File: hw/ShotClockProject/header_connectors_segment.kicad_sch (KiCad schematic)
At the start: 4 parts, among them J4 Conn_01x33_Pin, J5 Conn_01x33_Pin, J6 Conn_01x33_Pin, J7 Conn_01x33_Pin

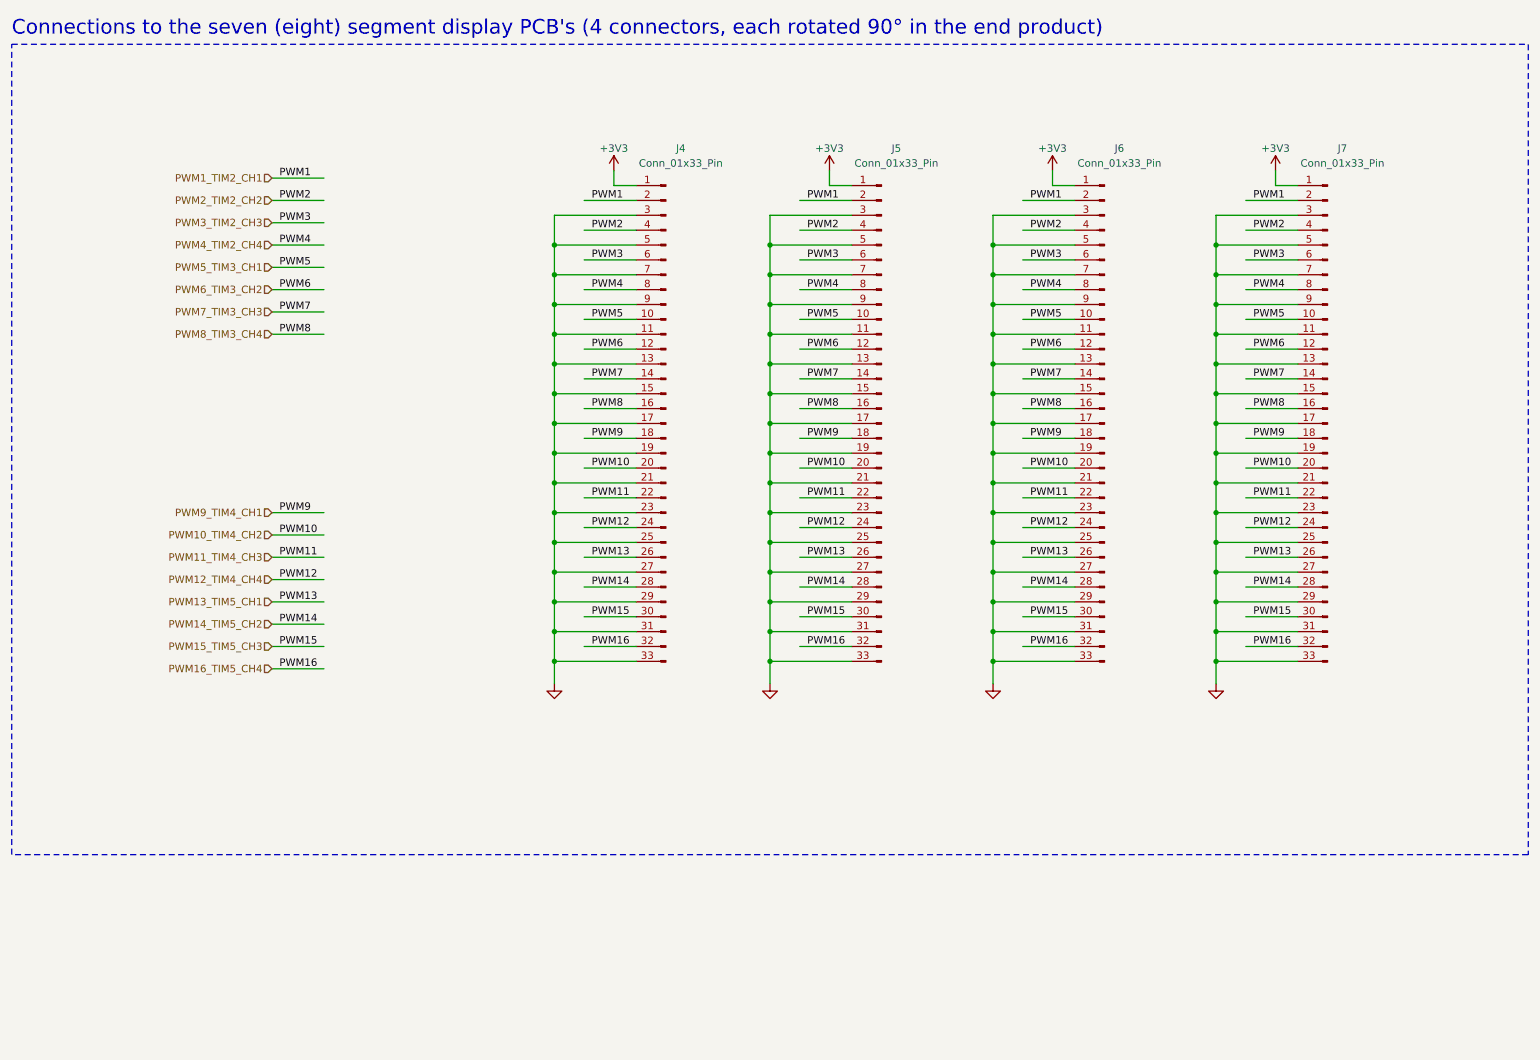
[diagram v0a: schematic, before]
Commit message: Fixed all ERC issues
Mainly by placing PWR_FLAGs and NetTies to show KiCAD where the GNDs are connected to each other physically, without them being the same net.
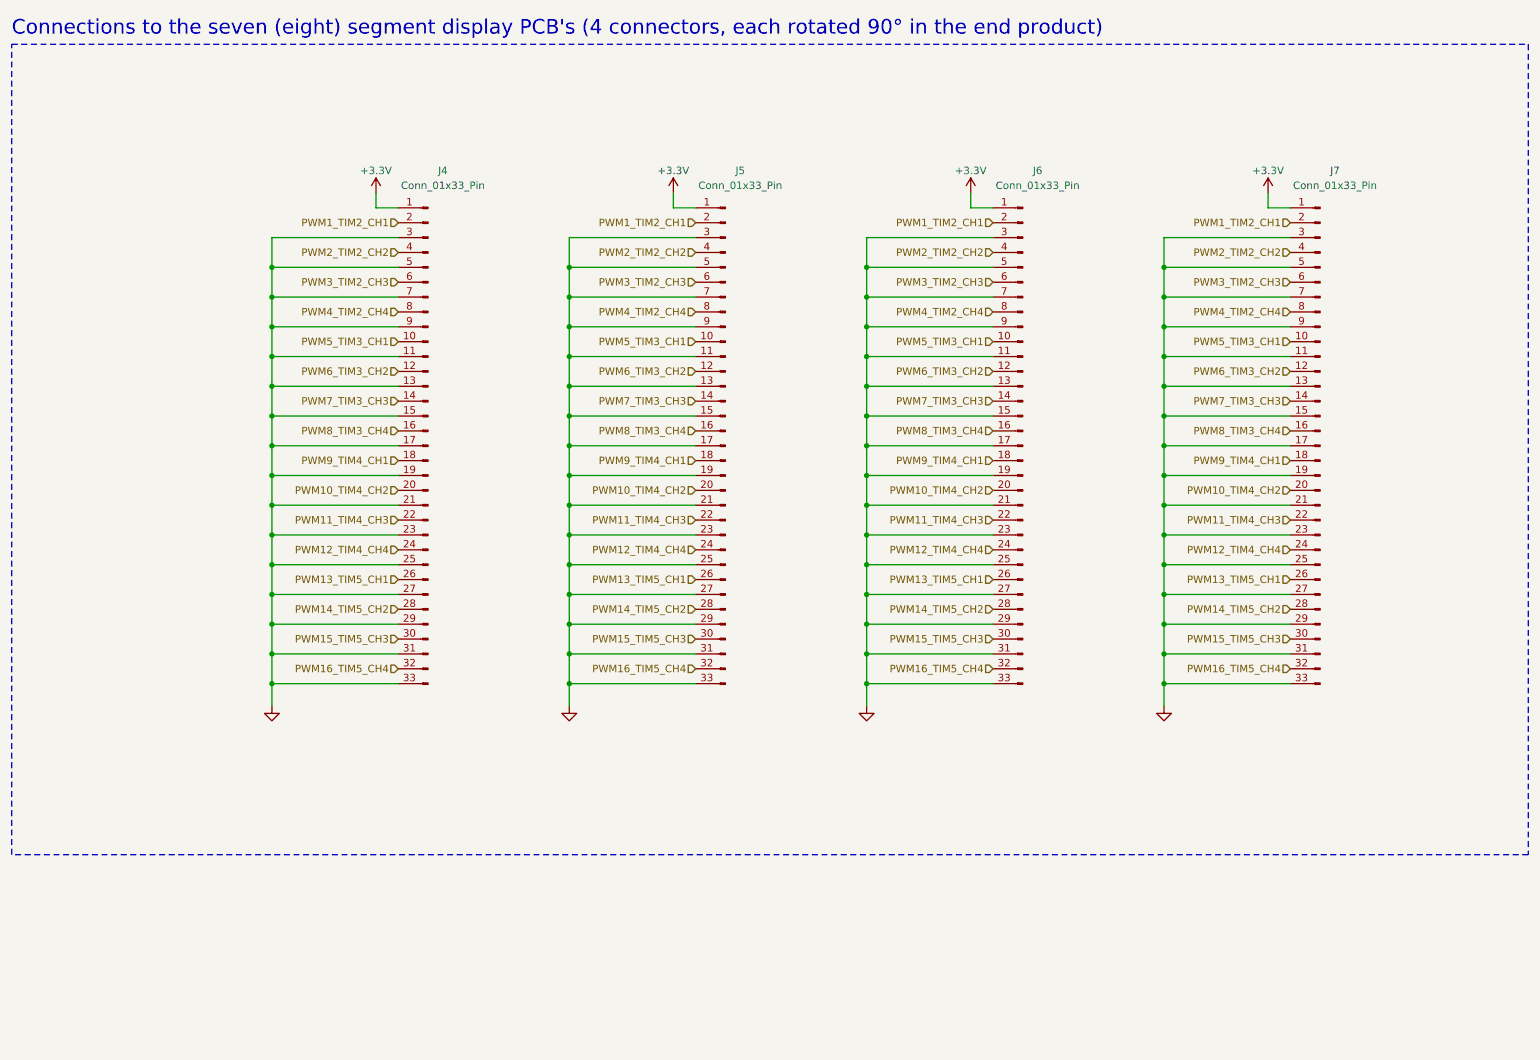
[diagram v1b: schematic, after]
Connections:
- net +3V3 renamed +3.3V
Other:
- title: (none) -> Shotclock Mainboard
- moved on the sheet: J4

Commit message: Finished footprint selection & updated design doc
Chosen all footprints
Updated design doc with part link & part selection reasons
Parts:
- J4, J5, J6, J7: footprint (none) -> Connector_PinHeader_2.54mm:PinHeader_1x33_P2.54mm_Horizontal
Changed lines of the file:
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@@
       (effects (font (size 1.27 1.27)))
     )
-    (property "Footprint" "" (at 90.17 91.44 0)
+    (property "Footprint" "Connector_PinHeader_2.54mm:PinHeader_1x33_P2.54mm_Horizontal" (at 90.17 91.44 0)
       (effects (font (size 1.27 1.27)) hide)
     )
@@
       (effects (font (size 1.27 1.27)))
     )
-    (property "Footprint" "" (at 191.77 91.44 0)
+    (property "Footprint" "Connector_PinHeader_2.54mm:PinHeader_1x33_P2.54mm_Horizontal" (at 191.77 91.44 0)
       (effects (font (size 1.27 1.27)) hide)
     )
@@
       (effects (font (size 1.27 1.27)))
     )
-    (property "Footprint" "" (at 242.57 91.44 0)
+    (property "Footprint" "Connector_PinHeader_2.54mm:PinHeader_1x33_P2.54mm_Horizontal" (at 242.57 91.44 0)
       (effects (font (size 1.27 1.27)) hide)
     )
@@
       (effects (font (size 1.27 1.27)))
     )
-    (property "Footprint" "" (at 140.97 91.44 0)
-      (effects (font (size 1.27 1.27)) hide)
-    )
+    (property "Footprint" "Connector_PinHeader_2.54mm:PinHeader_1x33_P2.54mm_Horizontal" (at 140.97 91.44 0)
+      (effects (font (size 1.27 1.27)) hide)
+    )

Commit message: Renamed references
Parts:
- renumbered J7 to J10, J4 to J7, J5 to J8, J6 to J9
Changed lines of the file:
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@@
         )
         (path "/5fd859aa-754d-49c2-9762-3f7ebe3bb64c/dbe9281d-d28a-4966-832c-4ef9ca7a9777"
-          (reference "#PWR047") (unit 1)
+          (reference "#PWR065") (unit 1)
         )
       )
@@
         )
         (path "/5fd859aa-754d-49c2-9762-3f7ebe3bb64c/dbe9281d-d28a-4966-832c-4ef9ca7a9777"
-          (reference "#PWR052") (unit 1)
+          (reference "#PWR068") (unit 1)
         )
       )
@@
         )
         (path "/5fd859aa-754d-49c2-9762-3f7ebe3bb64c/dbe9281d-d28a-4966-832c-4ef9ca7a9777"
-          (reference "#PWR046") (unit 1)
+          (reference "#PWR061") (unit 1)
         )
       )
@@
         )
         (path "/5fd859aa-754d-49c2-9762-3f7ebe3bb64c/dbe9281d-d28a-4966-832c-4ef9ca7a9777"
-          (reference "#PWR048") (unit 1)
+          (reference "#PWR066") (unit 1)
         )
       )
@@
   (symbol (lib_id "Connector:Conn_01x33_Pin") (at 90.17 91.44 0) (mirror y) (unit 1)
     (in_bom yes) (on_board yes) (dnp no)
-    (property "Reference" "J4" (at 92.71 44.45 0)
+    (property "Reference" "J7" (at 92.71 44.45 0)
       (effects (font (size 1.27 1.27)))
     )
@@
       (project "ShotClockProject"
         (path "/5fd859aa-754d-49c2-9762-3f7ebe3bb64c/dbe9281d-d28a-4966-832c-4ef9ca7a9777"
-          (reference "J4") (unit 1)
+          (reference "J7") (unit 1)
         )
       )
@@
   (symbol (lib_id "Connector:Conn_01x33_Pin") (at 191.77 91.44 0) (mirror y) (unit 1)
     (in_bom yes) (on_board yes) (dnp no)
-    (property "Reference" "J6" (at 194.31 44.45 0)
+    (property "Reference" "J9" (at 194.31 44.45 0)
       (effects (font (size 1.27 1.27)))
     )
@@
       (project "ShotClockProject"
         (path "/5fd859aa-754d-49c2-9762-3f7ebe3bb64c/dbe9281d-d28a-4966-832c-4ef9ca7a9777"
-          (reference "J6") (unit 1)
+          (reference "J9") (unit 1)
         )
       )
@@
         )
         (path "/5fd859aa-754d-49c2-9762-3f7ebe3bb64c/dbe9281d-d28a-4966-832c-4ef9ca7a9777"
-          (reference "#PWR049") (unit 1)
+          (reference "#PWR063") (unit 1)
         )
       )
@@
         )
         (path "/5fd859aa-754d-49c2-9762-3f7ebe3bb64c/dbe9281d-d28a-4966-832c-4ef9ca7a9777"
-          (reference "#PWR050") (unit 1)
+          (reference "#PWR067") (unit 1)
         )
       )
@@
         )
         (path "/5fd859aa-754d-49c2-9762-3f7ebe3bb64c/dbe9281d-d28a-4966-832c-4ef9ca7a9777"
-          (reference "#PWR051") (unit 1)
+          (reference "#PWR064") (unit 1)
         )
       )
@@
         )
         (path "/5fd859aa-754d-49c2-9762-3f7ebe3bb64c/dbe9281d-d28a-4966-832c-4ef9ca7a9777"
-          (reference "#PWR067") (unit 1)
+          (reference "#PWR062") (unit 1)
         )
       )
@@
   (symbol (lib_id "Connector:Conn_01x33_Pin") (at 242.57 91.44 0) (mirror y) (unit 1)
     (in_bom yes) (on_board yes) (dnp no)
-    (property "Reference" "J7" (at 245.11 44.45 0)
+    (property "Reference" "J10" (at 245.11 44.45 0)
       (effects (font (size 1.27 1.27)))
     )
@@
       (project "ShotClockProject"
         (path "/5fd859aa-754d-49c2-9762-3f7ebe3bb64c/dbe9281d-d28a-4966-832c-4ef9ca7a9777"
-          (reference "J7") (unit 1)
+          (reference "J10") (unit 1)
         )
       )
@@
   (symbol (lib_id "Connector:Conn_01x33_Pin") (at 140.97 91.44 0) (mirror y) (unit 1)
     (in_bom yes) (on_board yes) (dnp no)
-    (property "Reference" "J5" (at 143.51 44.45 0)
+    (property "Reference" "J8" (at 143.51 44.45 0)
       (effects (font (size 1.27 1.27)))
     )
@@
       (project "ShotClockProject"
         (path "/5fd859aa-754d-49c2-9762-3f7ebe3bb64c/dbe9281d-d28a-4966-832c-4ef9ca7a9777"
-          (reference "J5") (unit 1)
-        )
-      )
+          (reference "J8") (unit 1)
+        )
+      )

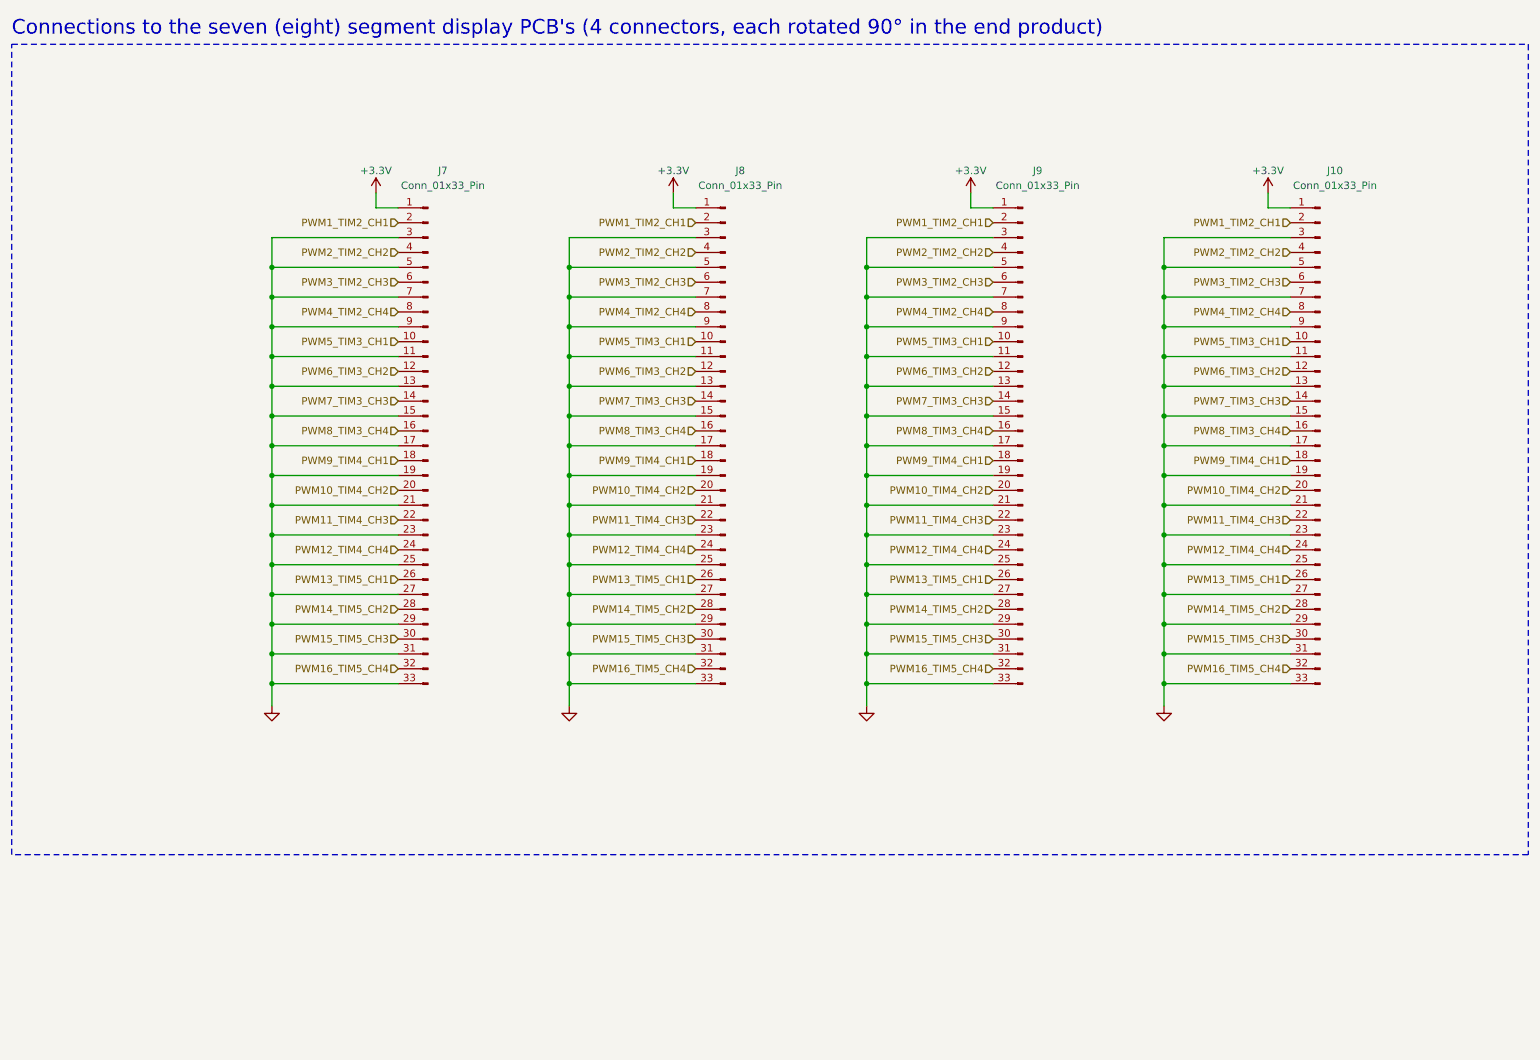
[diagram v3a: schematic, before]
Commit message: Changes headers, usb schematic and footprint
Now using standing USBc
Header & header pins are imported
All have 3d models now.

Removed fp-info-cache and added it to gitignore
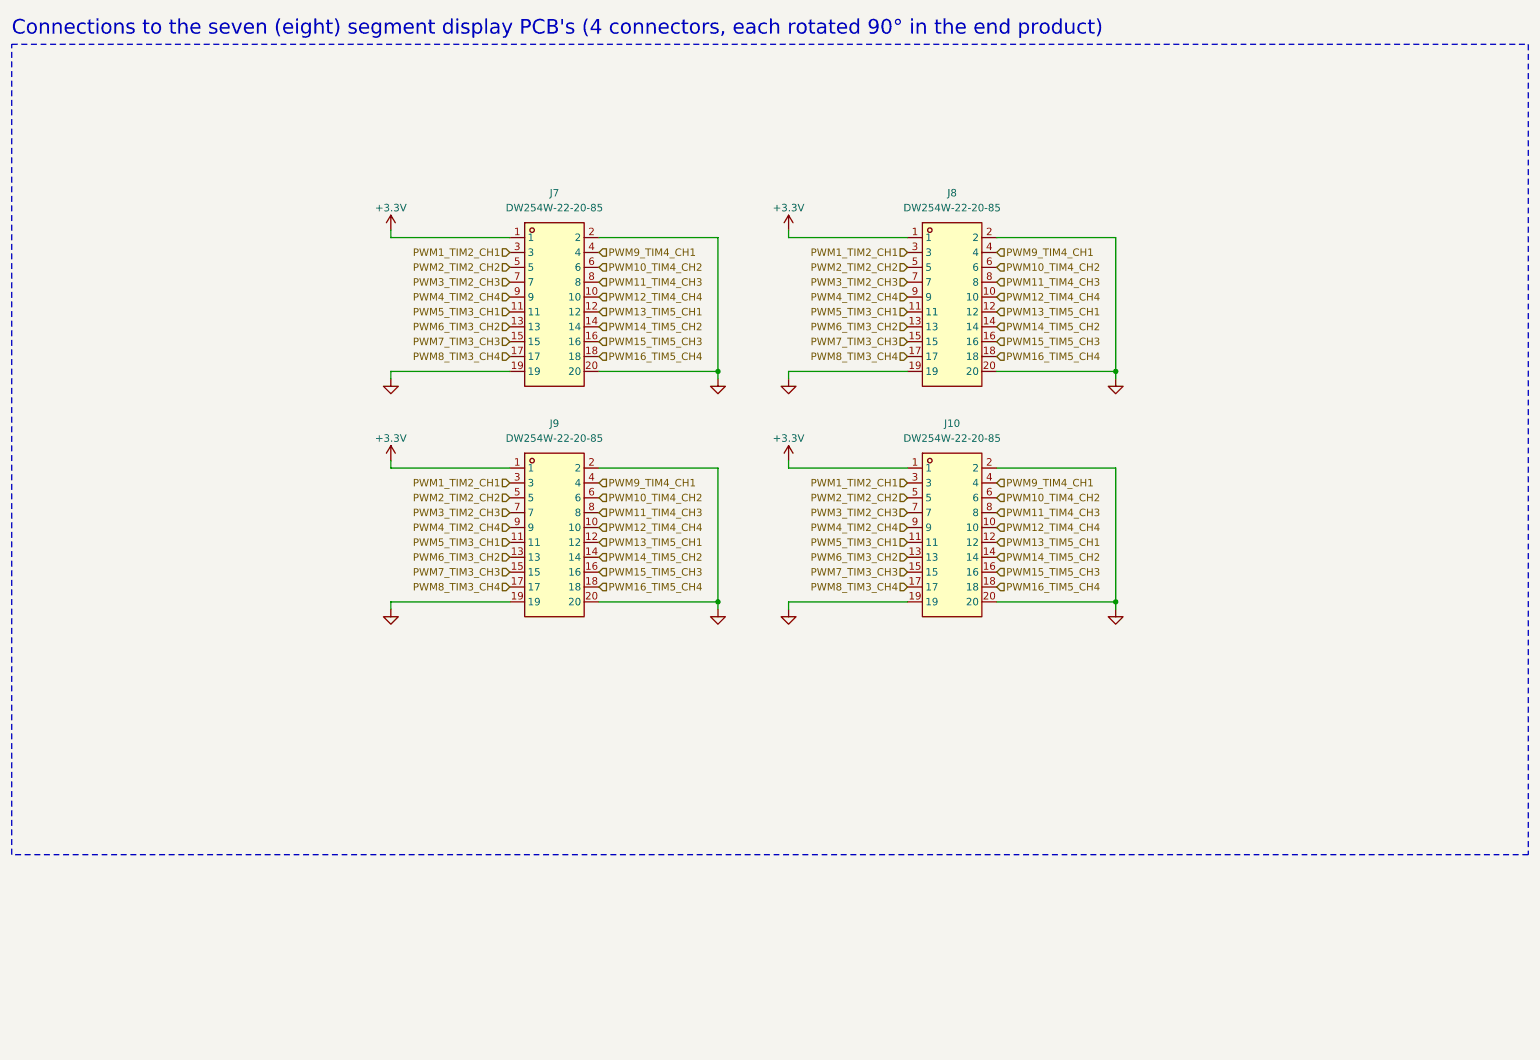
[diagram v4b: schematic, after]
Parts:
- removed J10, J7, J8, J9: Conn_01x33_Pin, Connector_PinHeader_2.54mm:PinHeader_1x33_P2.54mm_Horizontal, symbol Connector:Conn_01x33_Pin
- added J10, J7, J8, J9: DW254W-22-20-85, DW254W-22-20-85:CONN-TH_20P-P2.54_DEALON_DW254W-22-20-85, symbol DW254W-22-20-85:DW254W-22-20-85
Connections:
- net +3.3V: now also J10.1, J7.1, J8.1, J9.1
- net GND: now also J10.19, J10.2, J10.20, J7.19, J7.2, J7.20, J8.19, J8.2, J8.20, J9.19, J9.2, J9.20
- net PWM10_TIM4_CH2: now also J10.6, J7.6, J8.6, J9.6
- net PWM11_TIM4_CH3: now also J10.8, J7.8, J8.8, J9.8
- net PWM12_TIM4_CH4: now also J10.10, J7.10, J8.10, J9.10
- net PWM13_TIM5_CH1: now also J10.12, J7.12, J8.12, J9.12
- net PWM14_TIM5_CH2: now also J10.14, J7.14, J8.14, J9.14
- net PWM15_TIM5_CH3: now also J10.16, J7.16, J8.16, J9.16
- net PWM16_TIM5_CH4: now also J10.18, J7.18, J8.18, J9.18
- net PWM1_TIM2_CH1: now also J10.3, J7.3, J8.3, J9.3
- net PWM2_TIM2_CH2: now also J10.5, J7.5, J8.5, J9.5
- net PWM3_TIM2_CH3: now also J10.7, J7.7, J8.7, J9.7
- net PWM4_TIM2_CH4: now also J10.9, J7.9, J8.9, J9.9
- net PWM5_TIM3_CH1: now also J10.11, J7.11, J8.11, J9.11
- net PWM6_TIM3_CH2: now also J10.13, J7.13, J8.13, J9.13
- net PWM7_TIM3_CH3: now also J10.15, J7.15, J8.15, J9.15
- net PWM8_TIM3_CH4: now also J10.17, J7.17, J8.17, J9.17
- net PWM9_TIM4_CH1: now also J10.4, J7.4, J8.4, J9.4
